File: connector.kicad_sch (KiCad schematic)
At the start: 174 parts, among them J1 USB_C_Receptacle_USB2.0_16P, J10 POWER2, J11 TELEM1, J12 TELEM2, J13 GPS, J14 SERIAL4, J15 SERIAL5, J16 I2C, J17 CAN, J18 BUZZER, J19 Conn_01x05_Pin, J2 Micro_SD_Card_Det1, J20 ADC, J21 SPI, J22 SAFETY, J23 CAN2, J24 SBUS, J30 Channel 1, J31 Channel 2, J32 Channel 3, J33 Channel 4, J34 Channel 5, J35 Channel 6, J36 Channel 7, J37 Channel 8, J38 Channel 9, J39 Channel 13, J40 Channel 10, J53 Channel 14, J54 Channel 11, J55 Channel 15, J56 Channel 12, J57 Channel 16, J9 POWER1, Q1 AO3400A, U12 USBLC6-2SC6, U16 TPS2553DBVT, U17 TPS2553DBVT, U18 TPS2553DBVT, U19 TPS2553DBVT, U20 TPS2553DBVT, U21 TPS2553DBVT, U22 TPS2553DBVT, U23 TPS2553DBVT, U24 TPS2553DBVT

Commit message: Annotate: renumber total semua ref (Entire+Reset+X) — netlist 1009 node identik, ERC 0E/17W
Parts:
- renumbered C69 to C100, C72 to C101, C73 to C102, C62 to C103, C78 to C104, C76 to C105, C67 to C106, C65 to C107, C70 to C108, C71 to C109, C74 to C110, C75 to C111, C63 to C112, C79 to C113, C77 to C114, C125 to C62, C129 to C63, C133 to C64, C134 to C65, C82 to C66, C90 to C67, C124 to C68, C135 to C69, C126 to C70, C130 to C71, C136 to C72, C137 to C73, C84 to C74, C92 to C75, C138 to C76, C139 to C77, C112 to C78, C113 to C79, C127 to C80, C131 to C81, C140 to C82, C141 to C83, C86 to C84, C94 to C85, C142 to C86, C143 to C87, C114 to C88, C128 to C89, C132 to C90, C144 to C91, C145 to C92, C88 to C93, C96 to C94, C146 to C95, C147 to C96, C66 to C97, C64 to C98, C68 to C99, D5 to D7, J2 to J10, J18 to J11, J20 to J12, J17 to J13, J15 to J14, J22 to J15, J10 to J16, J16 to J17, J23 to J18, J30 to J19, J13 to J2, J34 to J20, J38 to J21, J39 to J22, J31 to J23, J35 to J24, J40 to J25, J53 to J26, J32 to J27, J36 to J28, J54 to J29, J21 to J3, J55 to J30, J33 to J31, J37 to J32, J56 to J33, J57 to J34, J11 to J4, J12 to J5, J24 to J6, J19 to J7, J14 to J8, R101 to R100, R99 to R101, R21 to R32, R59 to R33, R60 to R34, R51 to R35, R52 to R36, R53 to R37, R54 to R38, R55 to R39, R56 to R40, R57 to R41, R58 to R42, R22 to R43, R23 to R44, R19 to R45, R24 to R46, R20 to R47, R25 to R48, R47 to R49, R46 to R50, R61 to R51, R62 to R52, R48 to R53, R42 to R54, R43 to R55, R49 to R56, R50 to R57, R63 to R58, R64 to R59, R65 to R60, R66 to R61, R69 to R62, R44 to R63, R45 to R64, R70 to R65, R67 to R66, R68 to R67, R35 to R68, R39 to R69, R105 to R70, R106 to R71, R36 to R72, R40 to R73, R107 to R74, R108 to R75, R37 to R76, R41 to R77, R109 to R78, R110 to R79, R38 to R80, R104 to R81, R111 to R82, R112 to R83, R88 to R84, R86 to R85, R90 to R86, R91 to R87, R94 to R88, R95 to R89, R84 to R90, R100 to R91, R98 to R92, R89 to R93, R87 to R94, R92 to R95, R93 to R96, R96 to R97, R97 to R98, R85 to R99, U12 to U15, U18 to U16, U19 to U18, U20 to U19, U21 to U20, U22 to U21, U16 to U22, U24 to U23, U23 to U24

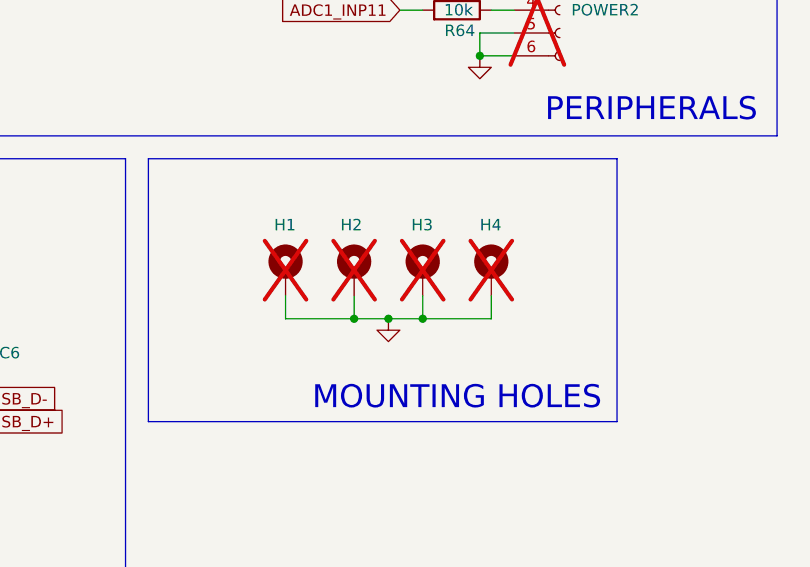
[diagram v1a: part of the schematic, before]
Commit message: Schematic: H1-H4 mounting hole -> isolated (Mechanical:MountingHole non-pad, wire+GND dihapus, footprint di-refill) — ERC 0E/17W, netlist 290/262/1005 (verified)
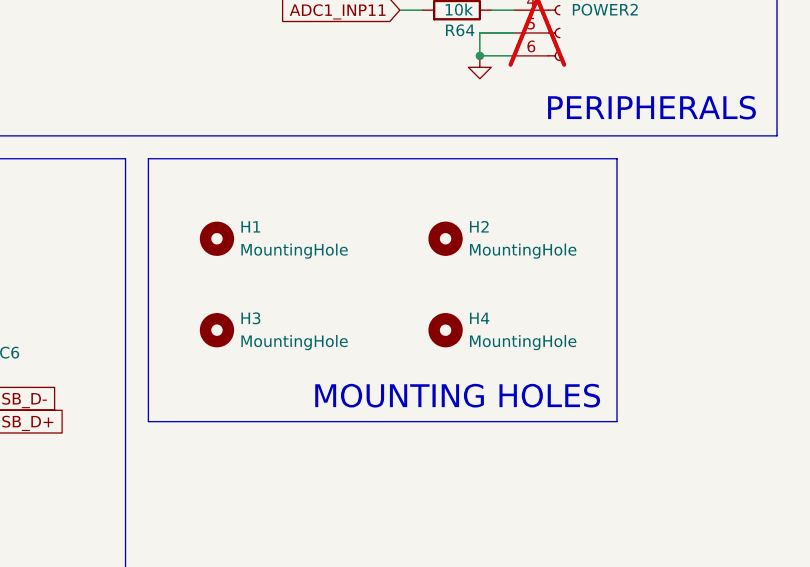
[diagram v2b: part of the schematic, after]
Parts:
- removed H1, H2, H3, H4: MountingHole_Pad, MountingHole:MountingHole_3.2mm_M3, symbol Mechanical:MountingHole_Pad
- added H1, H2, H3, H4: MountingHole, MountingHole:MountingHole_3.2mm_M3, symbol Mechanical:MountingHole

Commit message: Schematic: footprint 16 cap bank servo +VSERVO diisi (C66-C69/C74-C77/C84-C87/C93-C96 -> Capacitor_SMD:C_0603_1608Metric) — netlist 290/262/1005, ERC 0E/17W, diff 16 baris (verified); + bookkeeping pro/prl
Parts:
- C66, C67, C68, C69, C74, C75, C76, C77, C84, C85, C86, C87, C93, C94, C95, C96: footprint (none) -> Capacitor_SMD:C_0603_1608Metric
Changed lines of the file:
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@@
 			)
 		)
-		(property "Footprint" ""
+		(property "Footprint" "Capacitor_SMD:C_0603_1608Metric"
 			(at 252.4252 41.91 0)
 			(hide yes)
@@
 			)
 		)
-		(property "Footprint" ""
+		(property "Footprint" "Capacitor_SMD:C_0603_1608Metric"
 			(at 252.4252 92.71 0)
 			(hide yes)
@@
 			)
 		)
-		(property "Footprint" ""
+		(property "Footprint" "Capacitor_SMD:C_0603_1608Metric"
 			(at 303.2252 41.91 0)
 			(hide yes)
@@
 			)
 		)
-		(property "Footprint" ""
+		(property "Footprint" "Capacitor_SMD:C_0603_1608Metric"
 			(at 201.6252 92.71 0)
 			(hide yes)
@@
 			)
 		)
-		(property "Footprint" ""
+		(property "Footprint" "Capacitor_SMD:C_0603_1608Metric"
 			(at 303.2252 118.11 0)
 			(hide yes)
@@
 			)
 		)
-		(property "Footprint" ""
+		(property "Footprint" "Capacitor_SMD:C_0603_1608Metric"
 			(at 354.0252 118.11 0)
 			(hide yes)
@@
 			)
 		)
-		(property "Footprint" ""
+		(property "Footprint" "Capacitor_SMD:C_0603_1608Metric"
 			(at 252.4252 118.11 0)
 			(hide yes)
@@
 			)
 		)
-		(property "Footprint" ""
+		(property "Footprint" "Capacitor_SMD:C_0603_1608Metric"
 			(at 303.2252 67.31 0)
 			(hide yes)
@@
 			)
 		)
-		(property "Footprint" ""
+		(property "Footprint" "Capacitor_SMD:C_0603_1608Metric"
 			(at 201.6252 67.31 0)
 			(hide yes)
@@
 			)
 		)
-		(property "Footprint" ""
+		(property "Footprint" "Capacitor_SMD:C_0603_1608Metric"
 			(at 303.2252 92.71 0)
 			(hide yes)
@@
 			)
 		)
-		(property "Footprint" ""
+		(property "Footprint" "Capacitor_SMD:C_0603_1608Metric"
 			(at 354.0252 67.31 0)
 			(hide yes)
@@
 			)
 		)
-		(property "Footprint" ""
+		(property "Footprint" "Capacitor_SMD:C_0603_1608Metric"
 			(at 354.0252 41.91 0)
 			(hide yes)
@@
 			)
 		)
-		(property "Footprint" ""
+		(property "Footprint" "Capacitor_SMD:C_0603_1608Metric"
 			(at 201.6252 41.91 0)
 			(hide yes)
@@
 			)
 		)
-		(property "Footprint" ""
+		(property "Footprint" "Capacitor_SMD:C_0603_1608Metric"
 			(at 201.6252 118.11 0)
 			(hide yes)
@@
 			)
 		)
-		(property "Footprint" ""
+		(property "Footprint" "Capacitor_SMD:C_0603_1608Metric"
 			(at 354.0252 92.71 0)
 			(hide yes)
@@
 			)
 		)
-		(property "Footprint" ""
+		(property "Footprint" "Capacitor_SMD:C_0603_1608Metric"
 			(at 252.4252 67.31 0)
 			(hide yes)

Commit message: checkpoint: remap label TIM + swap silk servo (pre-F8)
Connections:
- net TIM1_CH1: now also R71.1; no longer R80.1
- net TIM1_CH2: now also R75.1; no longer R76.1
- net TIM1_CH3: now also R79.1; no longer R72.1
- net TIM2_CH1: now also R76.1; no longer R71.1
- net TIM2_CH2: now also R68.1; no longer R79.1
- net TIM2_CH3: now also R72.1; no longer R83.1
- net TIM3_CH2: now also R80.1; no longer R75.1
- net TIM3_CH3: now also R73.1; no longer R78.1
- net TIM3_CH4: now also R69.1; no longer R82.1
- net TIM4_CH2: now also R81.1; no longer R77.1
- net TIM4_CH3: now also R77.1; no longer R81.1
- net TIM5_CH1: now also R74.1; no longer R70.1
- net TIM5_CH2: now also R70.1; no longer R74.1
- net TIM8_CH1: now also R78.1; no longer R73.1
- net TIM8_CH2: now also R82.1; no longer R69.1
- net TIM8_CH4: now also R83.1; no longer R68.1

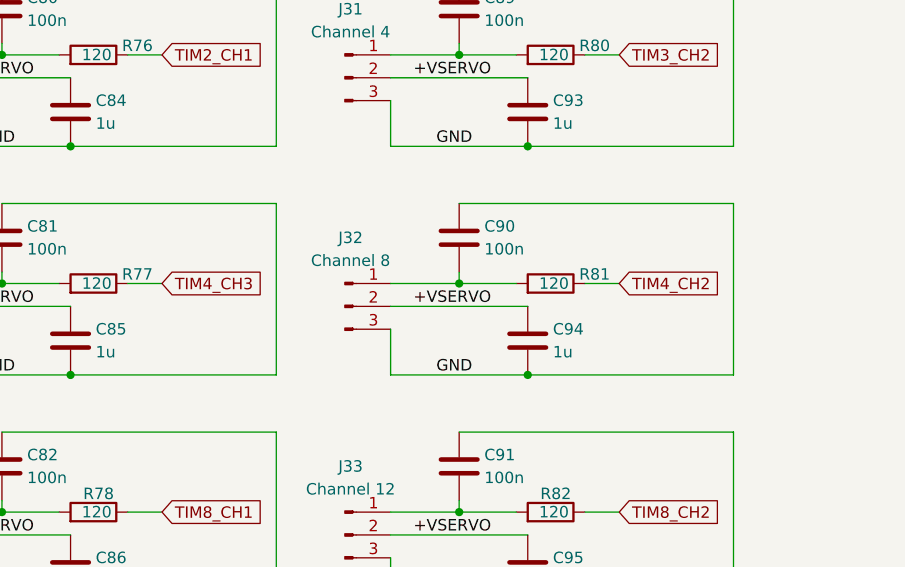
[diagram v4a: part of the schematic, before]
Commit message: Schematic: swap global label TIM4_CH2 <-> TIM4_CH3 (sheet Connector)
Perubahan: 2 global label ditukar di connector.kicad_sch.
Efek netlist: R77.1 TIM4_CH3->TIM4_CH2, R81.1 TIM4_CH2->TIM4_CH3;
pin MCU U1.M14/M15 tidak berubah, himpunan net identik (262=262).
Siap F8: kedua pad belum ada copper (0 track/via).
ERC 0E/17W (17 = lib_symbol_issues+lib_symbol_mismatch, verified kicad-cli).
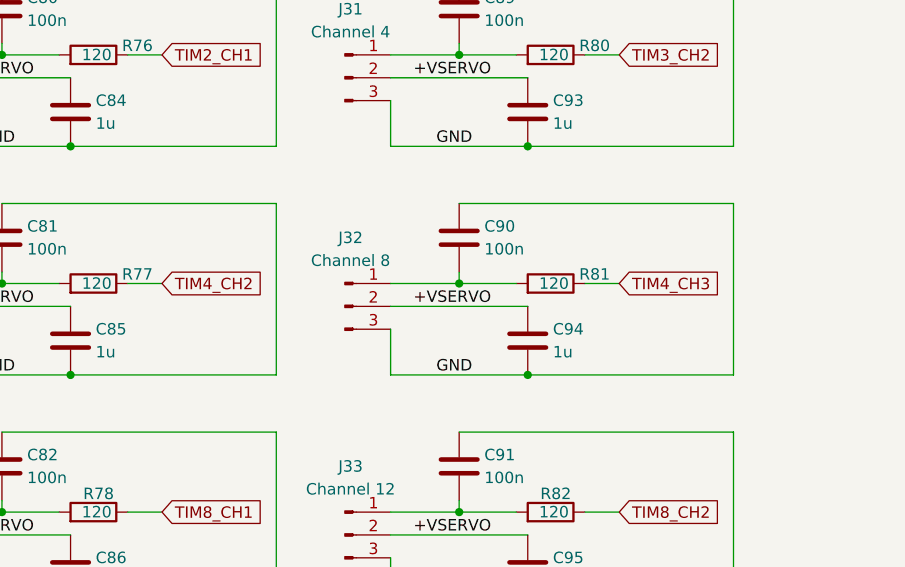
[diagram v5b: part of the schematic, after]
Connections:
- net TIM4_CH2: now also R77.1; no longer R81.1
- net TIM4_CH3: now also R81.1; no longer R77.1
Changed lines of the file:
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@@
 		)
 	)
-	(global_label "TIM4_CH2"
+	(global_label "TIM4_CH3"
 		(shape input)
 		(at 363.22 57.15 0)
@@
 		)
 	)
-	(global_label "TIM4_CH3"
+	(global_label "TIM4_CH2"
 		(shape input)
 		(at 312.42 57.15 0)
